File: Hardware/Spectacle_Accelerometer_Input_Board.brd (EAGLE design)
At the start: 25.4 x 55.9 mm, 47 parts, among them J2 FTDI_DEVICE, J3 AUDIO-JACK3, J4 AUDIO-JACK3, U1 CY8C4146LQI-S422, U2 3.3V/150mA, U3 ADXL345

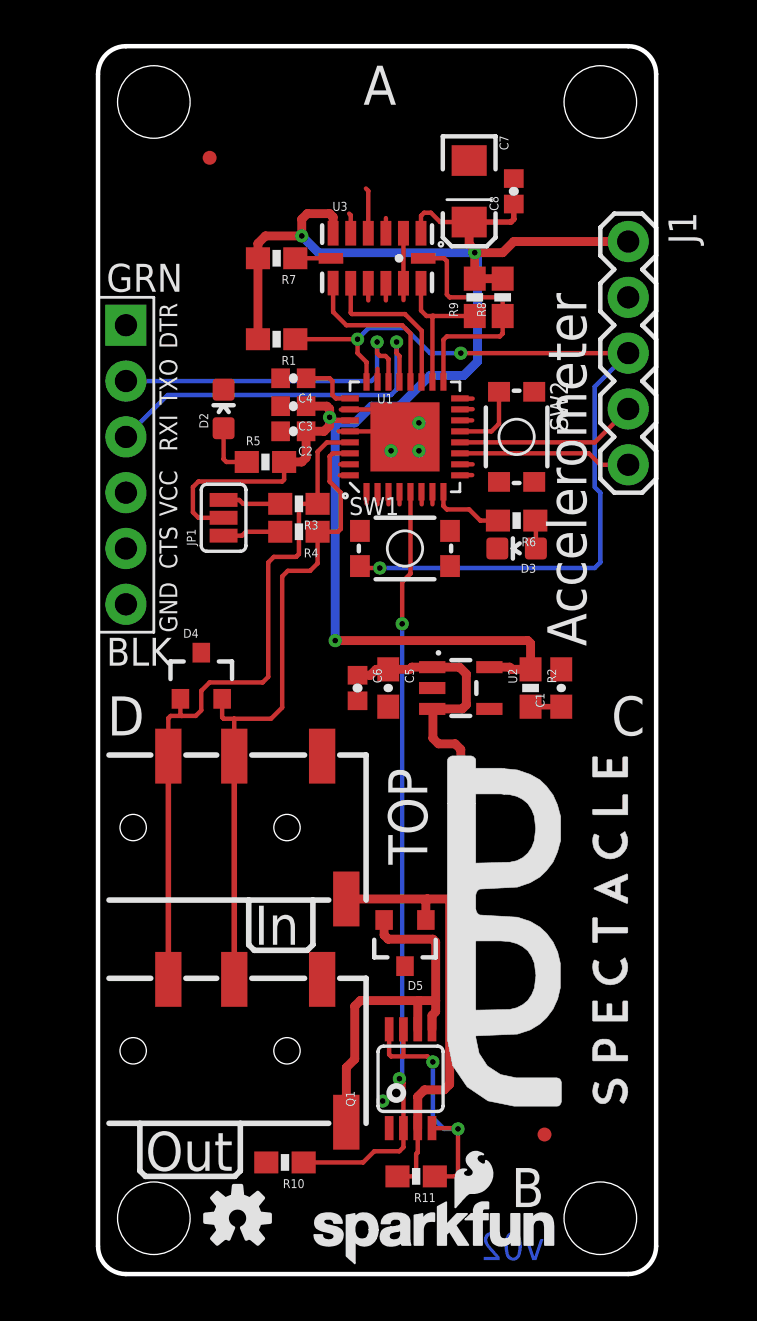
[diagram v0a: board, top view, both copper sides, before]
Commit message: I2C disconnect circuitry added
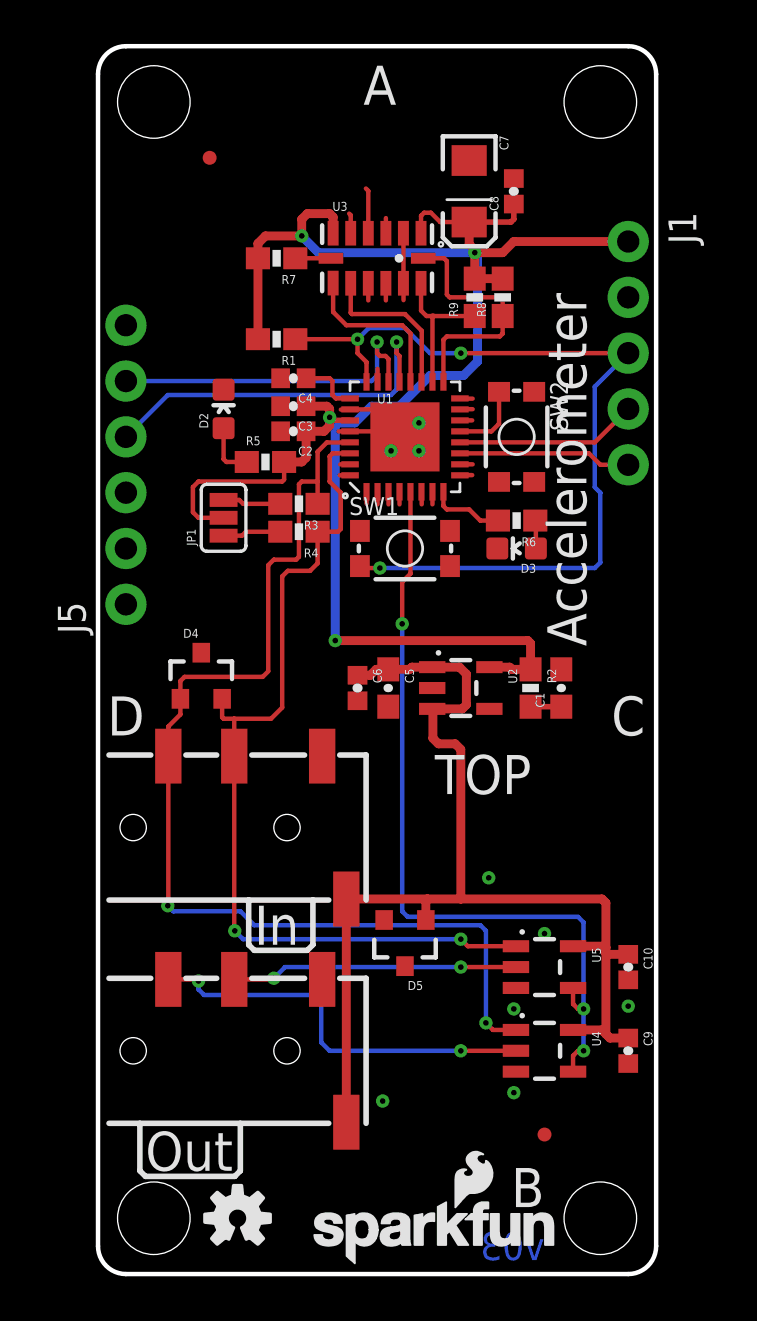
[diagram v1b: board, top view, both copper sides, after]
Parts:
- removed J2: FTDI_DEVICE, SparkFun-Connectors:FTDI_DEVICE_SIDE
- removed Q1: (no value), SparkFun-DiscreteSemi:MSOP8
- removed R10, R11: 10K, SparkFun-Resistors:0603-RES
- removed U$3: (no value), SparkFun-Aesthetics:SPECTACLE_LOGO_TITLE_0.35X0.70
- added C10, C9: 0.1uF, SparkFun-Capacitors:0402-CAP
- added J5: (no value), SparkFun-Connectors:1X06_NO_SILK
- added U4, U5: SN74LVC1G66, SparkFun-AnalogIC:SOT23-5
- J1: device SparkFun-Connectors:1X05 -> SparkFun-Connectors:1X05_NO_SILK
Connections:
- removed net N$37: Q1.4, Q1.7, Q1.8, R11.1
- removed net VOUT: D5.2, J4.EARTH, Q1.5, Q1.6
- removed net V_OUT_EN: Q1.2, R10.1, U1.5
- new net I2C_OUT_EN: U1.5, U4.4, U5.4
- new net SCL_OUT: J4.RING2, U4.2
- new net SDA_OUT: J4.RING1, U5.2
- net GND: now also C10.2, C9.2, J5.1, J5.2, U4.3, U5.3; no longer J2.P$5, J2.P$6, Q1.1, R10.2
- net RXI: now also J5.4; no longer J2.P$3
- net SCL: now also U4.1; no longer J4.RING2
- net SDA: now also U5.1; no longer J4.RING1
- net TXO: now also J5.5; no longer J2.P$2
- net VIN: now also C10.1, C9.1, J4.EARTH, U4.5, U5.5; no longer Q1.3, R11.2
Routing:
- net I2C_OUT_EN: track 0.00 -> 36.2 mm, vias 0 -> 3
- net V_OUT_EN: track 34.9 -> 0.00 mm, vias 2 -> 0
- net SCL_OUT: track 0.00 -> 18.5 mm, vias 0 -> 2
- net VOUT: track 17.8 -> 0.00 mm
- net SCL: track 32.4 -> 49.9 mm, vias 0 -> 2
- net VIN: track 38.5 -> 52.2 mm
- net SDA_OUT: track 0.00 -> 13.1 mm, vias 0 -> 2
- net N$37: track 12.8 -> 0.00 mm, vias 2 -> 0
- net SDA: track 30.7 -> 41.6 mm, vias 0 -> 2
- net GND: vias 4 -> 9
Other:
- board text added: "v03"
- board text removed: "v02"

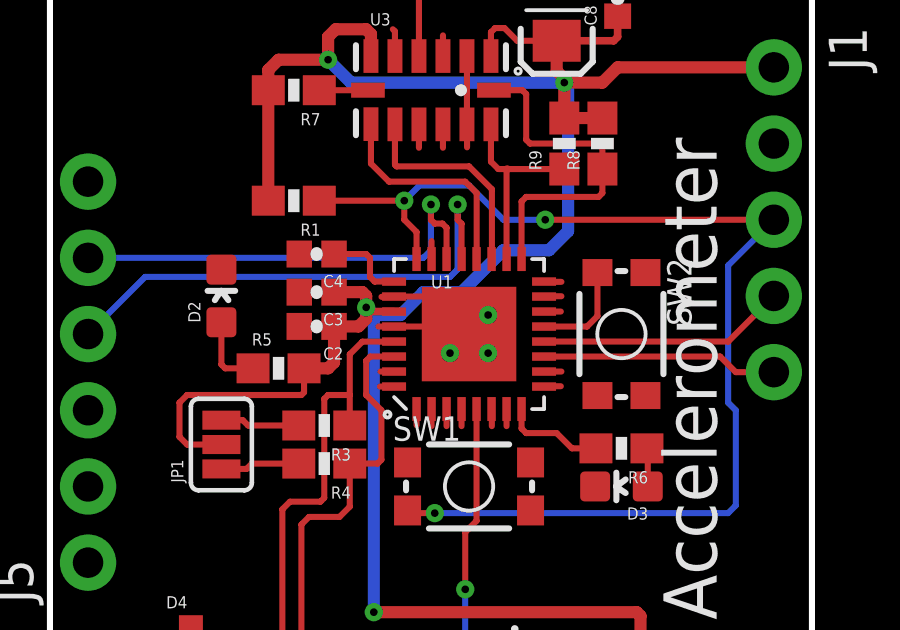
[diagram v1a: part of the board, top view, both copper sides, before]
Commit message: Change 2.2k I2C pullup to 4.7k Add Arduino test sketch
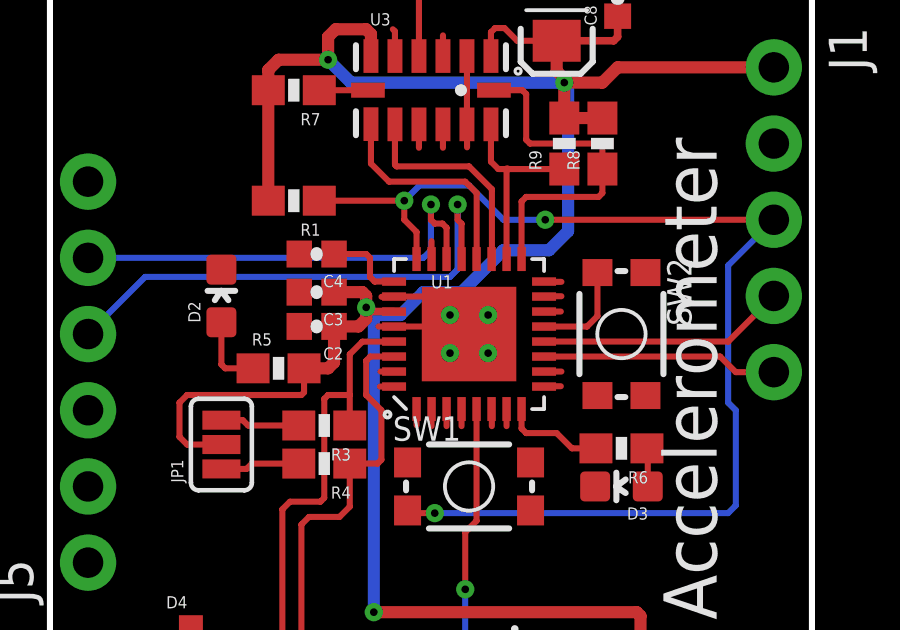
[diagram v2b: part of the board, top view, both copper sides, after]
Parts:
- R3, R4, R8, R9: value 2.2k -> 4.7K
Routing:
- net GND: vias 9 -> 10
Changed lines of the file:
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@@
 <layers>
 <layer number="1" name="Top" color="4" fill="1" visible="yes" active="yes"/>
-<layer number="2" name="Route2" color="1" fill="3" visible="no" active="yes"/>
-<layer number="15" name="Route15" color="4" fill="6" visible="no" active="yes"/>
+<layer number="2" name="Route2" color="1" fill="3" visible="yes" active="yes"/>
+<layer number="15" name="Route15" color="4" fill="6" visible="yes" active="yes"/>
 <layer number="16" name="Bottom" color="1" fill="1" visible="yes" active="yes"/>
 <layer number="17" name="Pads" color="2" fill="1" visible="yes" active="yes"/>
@@
 <layer number="23" name="tOrigins" color="15" fill="1" visible="yes" active="yes"/>
 <layer number="24" name="bOrigins" color="15" fill="1" visible="yes" active="yes"/>
-<layer number="25" name="tNames" color="7" fill="1" visible="no" active="yes"/>
-<layer number="26" name="bNames" color="7" fill="1" visible="no" active="yes"/>
-<layer number="27" name="tValues" color="7" fill="1" visible="no" active="yes"/>
-<layer number="28" name="bValues" color="7" fill="1" visible="no" active="yes"/>
-<layer number="29" name="tStop" color="7" fill="3" visible="no" active="yes"/>
-<layer number="30" name="bStop" color="7" fill="6" visible="no" active="yes"/>
-<layer number="31" name="tCream" color="7" fill="4" visible="no" active="yes"/>
-<layer number="32" name="bCream" color="7" fill="5" visible="no" active="yes"/>
-<layer number="39" name="tKeepout" color="4" fill="11" visible="no" active="yes"/>
-<layer number="40" name="bKeepout" color="1" fill="11" visible="no" active="yes"/>
-<layer number="41" name="tRestrict" color="4" fill="10" visible="no" active="yes"/>
-<layer number="42" name="bRestrict" color="1" fill="10" visible="no" active="yes"/>
-<layer number="43" name="vRestrict" color="2" fill="10" visible="no" active="yes"/>
-<layer number="44" name="Drills" color="7" fill="1" visible="no" active="yes"/>
+<layer number="25" name="tNames" color="7" fill="1" visible="yes" active="yes"/>
+<layer number="26" name="bNames" color="7" fill="1" visible="yes" active="yes"/>
+<layer number="27" name="tValues" color="7" fill="1" visible="yes" active="yes"/>
+<layer number="28" name="bValues" color="7" fill="1" visible="yes" active="yes"/>
+<layer number="29" name="tStop" color="7" fill="3" visible="yes" active="yes"/>
+<layer number="30" name="bStop" color="7" fill="6" visible="yes" active="yes"/>
+<layer number="31" name="tCream" color="7" fill="4" visible="yes" active="yes"/>
+<layer number="32" name="bCream" color="7" fill="5" visible="yes" active="yes"/>
+<layer number="39" name="tKeepout" color="4" fill="11" visible="yes" active="yes"/>
+<layer number="40" name="bKeepout" color="1" fill="11" visible="yes" active="yes"/>
+<layer number="41" name="tRestrict" color="4" fill="10" visible="yes" active="yes"/>
+<layer number="42" name="bRestrict" color="1" fill="10" visible="yes" active="yes"/>
+<layer number="43" name="vRestrict" color="2" fill="10" visible="yes" active="yes"/>
+<layer number="44" name="Drills" color="7" fill="1" visible="yes" active="yes"/>
 <layer number="45" name="Holes" color="7" fill="1" visible="yes" active="yes"/>
-<layer number="46" name="Milling" color="3" fill="1" visible="no" active="yes"/>
-<layer number="47" name="Measures" color="7" fill="1" visible="no" active="yes"/>
-<layer number="48" name="Document" color="7" fill="1" visible="no" active="yes"/>
-<layer number="49" name="Reference" color="7" fill="1" visible="no" active="yes"/>
+<layer number="46" name="Milling" color="3" fill="1" visible="yes" active="yes"/>
+<layer number="47" name="Measures" color="7" fill="1" visible="yes" active="yes"/>
+<layer number="48" name="Document" color="7" fill="1" visible="yes" active="yes"/>
+<layer number="49" name="Reference" color="7" fill="1" visible="yes" active="yes"/>
 <layer number="51" name="tDocu" color="6" fill="1" visible="yes" active="yes"/>
-<layer number="52" name="bDocu" color="7" fill="1" visible="no" active="yes"/>
+<layer number="52" name="bDocu" color="7" fill="1" visible="yes" active="yes"/>
 <layer number="3" name="Route3" color="4" fill="3" visible="no" active="no"/>
 <layer number="4" name="Route4" color="1" fill="4" visible="no" active="no"/>
@@
 <attribute name="PROD_ID" value="CAP-12416" x="11.811" y="26.67" size="1.778" layer="27" font="vector" ratio="15" rot="R270" display="off"/>
 </element>
-<element name="R3" library="SparkFun-Resistors" package="0603-RES" value="2.2k" x="9.144" y="35.052" rot="R180">
-<attribute name="PROD_ID" value="RES-08272" x="9.144" y="35.052" size="1.778" layer="27" font="vector" ratio="15" rot="R180" display="off"/>
-</element>
-<element name="R4" library="SparkFun-Resistors" package="0603-RES" value="2.2k" x="9.144" y="33.782" rot="R180">
-<attribute name="PROD_ID" value="RES-08272" x="9.144" y="33.782" size="1.778" layer="27" font="vector" ratio="15" rot="R180" display="off"/>
+<element name="R3" library="SparkFun-Resistors" package="0603-RES" value="4.7K" x="9.144" y="35.052" rot="R180">
+<attribute name="PROD_ID" value="RES-07857" x="9.144" y="35.052" size="1.778" layer="27" font="vector" ratio="15" rot="R180" display="off"/>
+</element>
+<element name="R4" library="SparkFun-Resistors" package="0603-RES" value="4.7K" x="9.144" y="33.782" rot="R180">
+<attribute name="PROD_ID" value="RES-07857" x="9.144" y="33.782" size="1.778" layer="27" font="vector" ratio="15" rot="R180" display="off"/>
 </element>
 <element name="JP1" library="SparkFun-Passives" package="PAD-JUMPER-3-NC_BY_PASTE_YES_SILK_FULL_BOX" value="JUMPER-PAD-3-NC_BY_PASTE" x="5.715" y="34.417" rot="R90"/>
@@
 <attribute name="PROD_ID" value="CAP-12416" x="18.923" y="49.276" size="1.778" layer="27" font="vector" ratio="15" rot="R90" display="off"/>
 </element>
-<element name="R8" library="SparkFun-Resistors" package="0603-RES" value="2.2k" x="18.415" y="44.45" rot="R90">
-<attribute name="PROD_ID" value="RES-08272" x="18.415" y="44.45" size="1.778" layer="27" font="vector" ratio="15" rot="R90" display="off"/>
-</element>
-<element name="R9" library="SparkFun-Resistors" package="0603-RES" value="2.2k" x="17.145" y="44.45" rot="R90">
-<attribute name="PROD_ID" value="RES-08272" x="17.145" y="44.45" size="1.778" layer="27" font="vector" ratio="15" rot="R90" display="off"/>
+<element name="R8" library="SparkFun-Resistors" package="0603-RES" value="4.7K" x="18.415" y="44.45" rot="R90">
+<attribute name="PROD_ID" value="RES-07857" x="18.415" y="44.45" size="1.778" layer="27" font="vector" ratio="15" rot="R90" display="off"/>
+</element>
+<element name="R9" library="SparkFun-Resistors" package="0603-RES" value="4.7K" x="17.145" y="44.45" rot="R90">
+<attribute name="PROD_ID" value="RES-07857" x="17.145" y="44.45" size="1.778" layer="27" font="vector" ratio="15" rot="R90" display="off"/>
 </element>
 <element name="H1" library="SparkFun-Electromechanical" package="STAND-OFF" value="STAND-OFF" x="22.86" y="53.34"/>
@@
 <via x="17.78" y="18.034" extent="1-16" drill="0.254"/>
 <via x="20.32" y="15.494" extent="1-16" drill="0.254"/>
+<via x="13.335" y="38.735" extent="1-16" drill="0.254"/>
 </signal>
 <signal name="VCC">

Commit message: Touch-ups for v10 release
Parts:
- J3, J4: value AUDIO-JACK3 -> AUDIO_JACK_TRRSSMD_RA; device SparkFun-Connectors:AUDIO-JACK-TRRS-SMD -> SparkFun-Connectors:AUDIO_JACK_3.5MM_TRRS_SMD_RA
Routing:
- net I2C_OUT_EN: track 36.2 -> 37.7 mm
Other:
- board text added: "v10"
- board text removed: "v03"
